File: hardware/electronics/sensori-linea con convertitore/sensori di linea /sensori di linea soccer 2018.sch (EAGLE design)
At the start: 27 parts, among them T1 BP103, T2 BP103, T3 BP103, T4 BP103

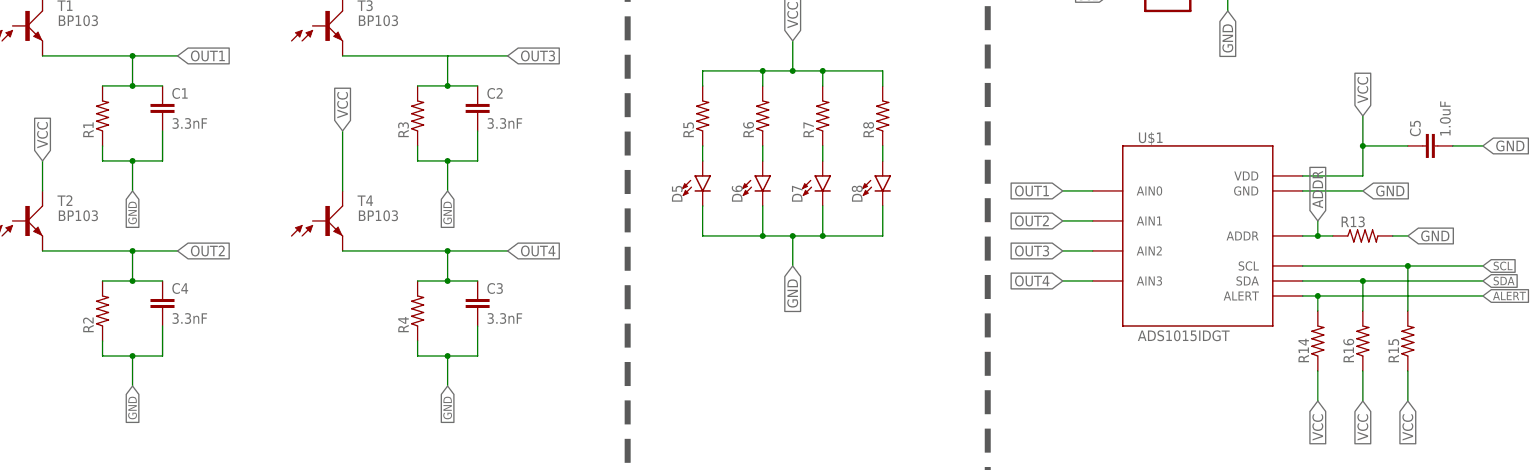
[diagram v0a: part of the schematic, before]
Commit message: sensori di linea completi 2018
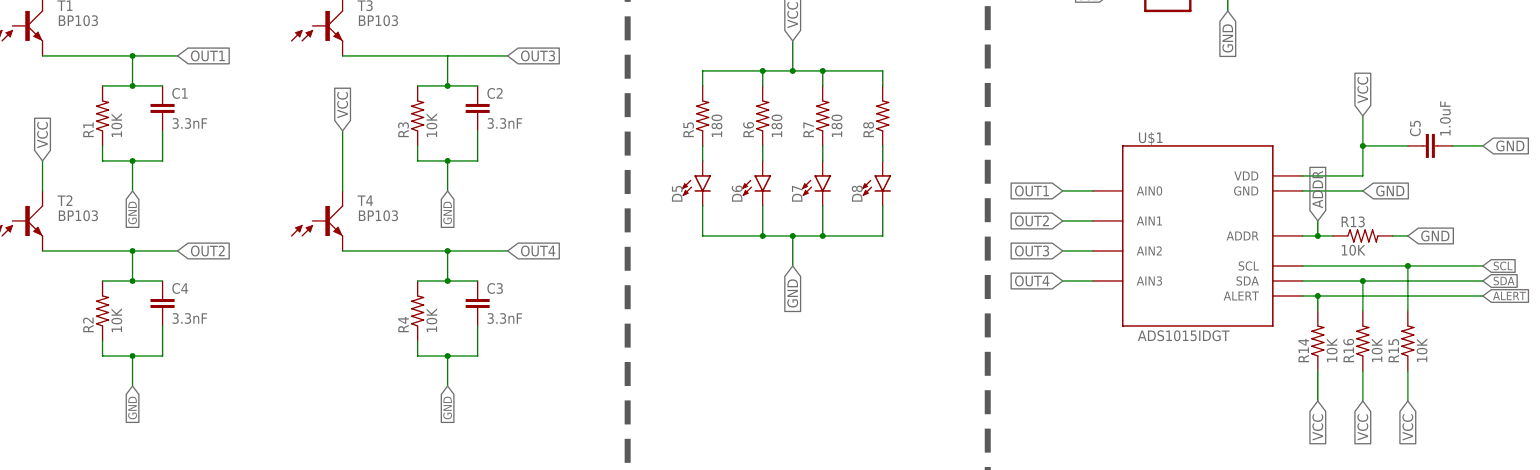
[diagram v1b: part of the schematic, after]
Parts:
- R1, R13, R14, R15, R16, R2, R3, R4: value (none) -> 10K
- R5, R6, R7: value (none) -> 180
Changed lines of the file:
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@@
 <part name="T3" library="opto-trans-siemens" library_urn="urn:adsk.eagle:library:317" deviceset="BP103" device="" package3d_urn="urn:adsk.eagle:package:21787/1"/>
 <part name="T4" library="opto-trans-siemens" library_urn="urn:adsk.eagle:library:317" deviceset="BP103" device="" package3d_urn="urn:adsk.eagle:package:21787/1"/>
-<part name="R1" library="resistor" library_urn="urn:adsk.eagle:library:348" deviceset="R-US_" device="0204/7" package3d_urn="urn:adsk.eagle:package:25945/1"/>
-<part name="R2" library="resistor" library_urn="urn:adsk.eagle:library:348" deviceset="R-US_" device="0204/7" package3d_urn="urn:adsk.eagle:package:25945/1"/>
-<part name="R3" library="resistor" library_urn="urn:adsk.eagle:library:348" deviceset="R-US_" device="0204/7" package3d_urn="urn:adsk.eagle:package:25945/1"/>
-<part name="R4" library="resistor" library_urn="urn:adsk.eagle:library:348" deviceset="R-US_" device="0204/7" package3d_urn="urn:adsk.eagle:package:25945/1"/>
-<part name="R5" library="rcl" library_urn="urn:adsk.eagle:library:334" deviceset="R-US_" device="0204/7" package3d_urn="urn:adsk.eagle:package:23498/1"/>
-<part name="R6" library="rcl" library_urn="urn:adsk.eagle:library:334" deviceset="R-US_" device="0204/7" package3d_urn="urn:adsk.eagle:package:23498/1"/>
-<part name="R7" library="rcl" library_urn="urn:adsk.eagle:library:334" deviceset="R-US_" device="0204/7" package3d_urn="urn:adsk.eagle:package:23498/1"/>
+<part name="R1" library="resistor" library_urn="urn:adsk.eagle:library:348" deviceset="R-US_" device="0204/7" package3d_urn="urn:adsk.eagle:package:25945/1" value="10K"/>
+<part name="R2" library="resistor" library_urn="urn:adsk.eagle:library:348" deviceset="R-US_" device="0204/7" package3d_urn="urn:adsk.eagle:package:25945/1" value="10K"/>
+<part name="R3" library="resistor" library_urn="urn:adsk.eagle:library:348" deviceset="R-US_" device="0204/7" package3d_urn="urn:adsk.eagle:package:25945/1" value="10K"/>
+<part name="R4" library="resistor" library_urn="urn:adsk.eagle:library:348" deviceset="R-US_" device="0204/7" package3d_urn="urn:adsk.eagle:package:25945/1" value="10K"/>
+<part name="R5" library="rcl" library_urn="urn:adsk.eagle:library:334" deviceset="R-US_" device="0204/7" package3d_urn="urn:adsk.eagle:package:23498/1" value="180"/>
+<part name="R6" library="rcl" library_urn="urn:adsk.eagle:library:334" deviceset="R-US_" device="0204/7" package3d_urn="urn:adsk.eagle:package:23498/1" value="180"/>
+<part name="R7" library="rcl" library_urn="urn:adsk.eagle:library:334" deviceset="R-US_" device="0204/7" package3d_urn="urn:adsk.eagle:package:23498/1" value="180"/>
 <part name="R8" library="rcl" library_urn="urn:adsk.eagle:library:334" deviceset="R-US_" device="0204/7" package3d_urn="urn:adsk.eagle:package:23498/1"/>
 <part name="SV1" library="con-lstb" library_urn="urn:adsk.eagle:library:162" deviceset="MA03-2" device="" package3d_urn="urn:adsk.eagle:package:8334/1"/>
@@
 <part name="U$1" library="bt_adc" deviceset="ADS1015" device="IDGT"/>
 <part name="C5" library="SparkFun-Capacitors" deviceset="1.0UF" device="-0402-16V-10%" value="1.0uF"/>
-<part name="R13" library="resistor" library_urn="urn:adsk.eagle:library:348" deviceset="R-US_" device="0204/7" package3d_urn="urn:adsk.eagle:package:25945/1"/>
-<part name="R14" library="resistor" library_urn="urn:adsk.eagle:library:348" deviceset="R-US_" device="0204/7" package3d_urn="urn:adsk.eagle:package:25945/1"/>
-<part name="R15" library="resistor" library_urn="urn:adsk.eagle:library:348" deviceset="R-US_" device="0204/7" package3d_urn="urn:adsk.eagle:package:25945/1"/>
-<part name="R16" library="resistor" library_urn="urn:adsk.eagle:library:348" deviceset="R-US_" device="0204/7" package3d_urn="urn:adsk.eagle:package:25945/1"/>
+<part name="R13" library="resistor" library_urn="urn:adsk.eagle:library:348" deviceset="R-US_" device="0204/7" package3d_urn="urn:adsk.eagle:package:25945/1" value="10K"/>
+<part name="R14" library="resistor" library_urn="urn:adsk.eagle:library:348" deviceset="R-US_" device="0204/7" package3d_urn="urn:adsk.eagle:package:25945/1" value="10K"/>
+<part name="R15" library="resistor" library_urn="urn:adsk.eagle:library:348" deviceset="R-US_" device="0204/7" package3d_urn="urn:adsk.eagle:package:25945/1" value="10K"/>
+<part name="R16" library="resistor" library_urn="urn:adsk.eagle:library:348" deviceset="R-US_" device="0204/7" package3d_urn="urn:adsk.eagle:package:25945/1" value="10K"/>
 </parts>
 <sheets>
